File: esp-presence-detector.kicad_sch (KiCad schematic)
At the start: 6 parts, among them J1 AM312 female header, J2 LDR female header, U1 Wemos NodeMCU, U2 AM312

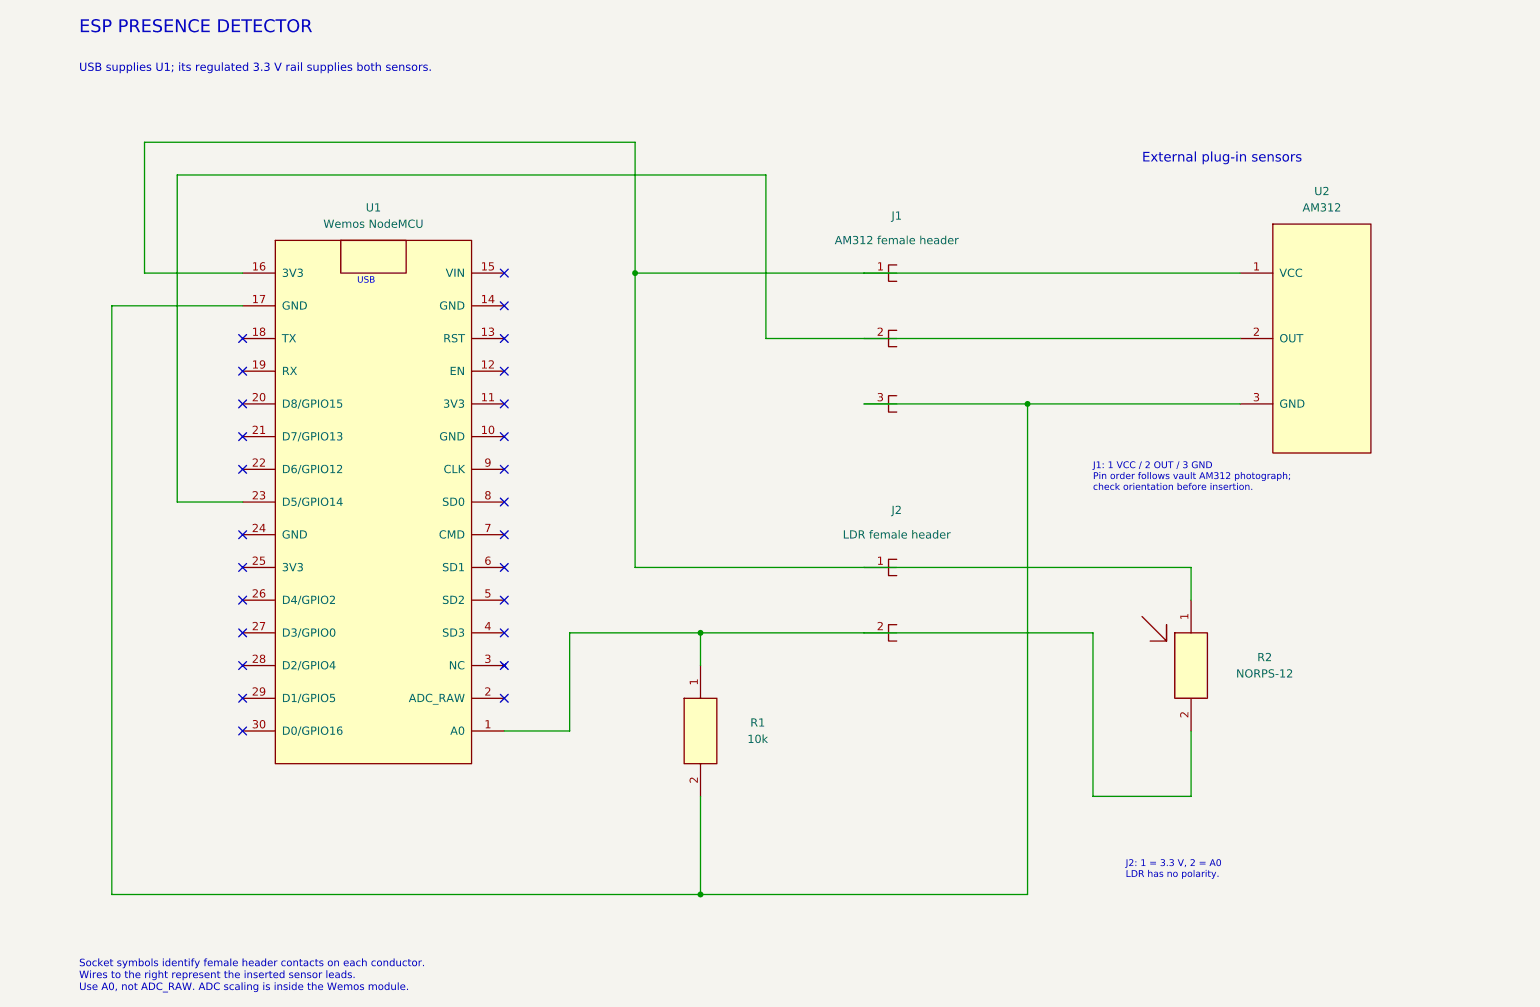
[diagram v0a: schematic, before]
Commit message: refactor: simplify schematic power and sensor connections
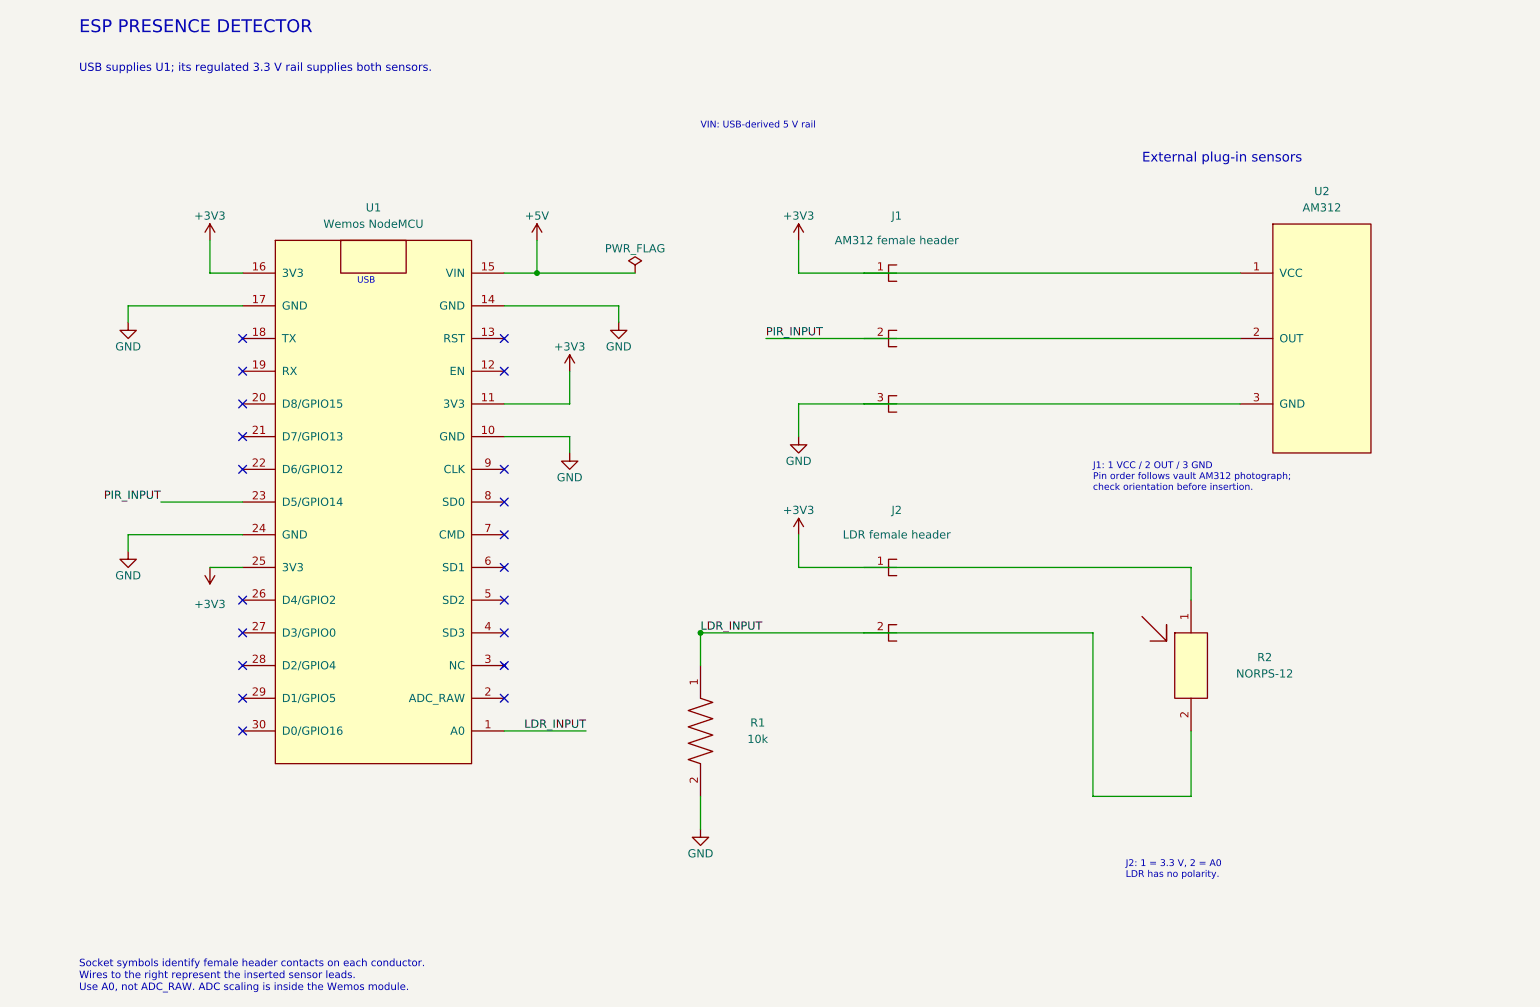
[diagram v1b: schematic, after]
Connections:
- net +3V3: now reaches J1.1, J2.1, R2.1, U1.16 (3V3), U2.1 (VCC)
- net +3V3: now also U1.11 (3V3), U1.25 (3V3)
- net PIR_INPUT: now reaches J1.2, U1.23 (D5/GPIO14), U2.2 (OUT)
- net GND: now reaches J1.3, R1.2, U1.17 (GND), U2.3 (GND)
- net GND: now also U1.10 (GND), U1.14 (GND), U1.24 (GND)
- net LDR_INPUT: now reaches J2.2, R1.1, R2.2, U1.1 (A0)
- net +5V: now reaches U1.15 (VIN)
- no-connect marks 26 -> 20
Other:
- note added: "VIN: USB-derived 5 V rail"

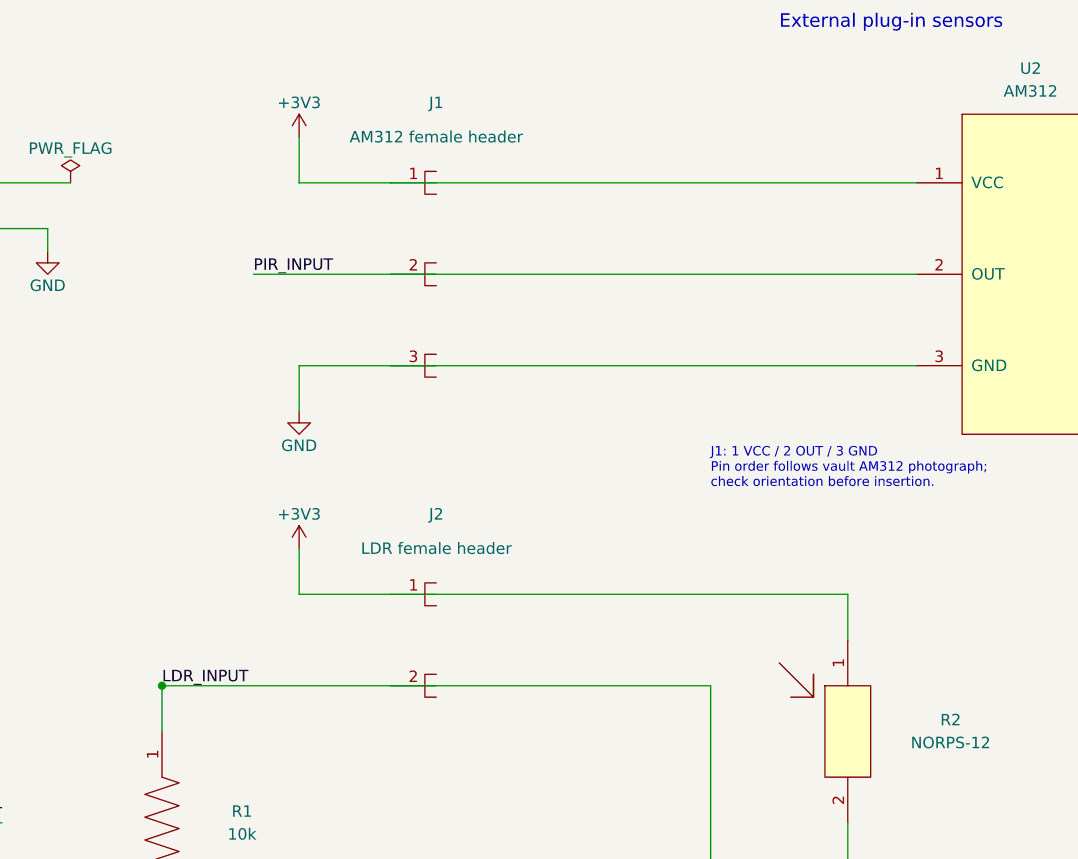
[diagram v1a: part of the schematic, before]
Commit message: refactor: use standard KiCad socket connectors
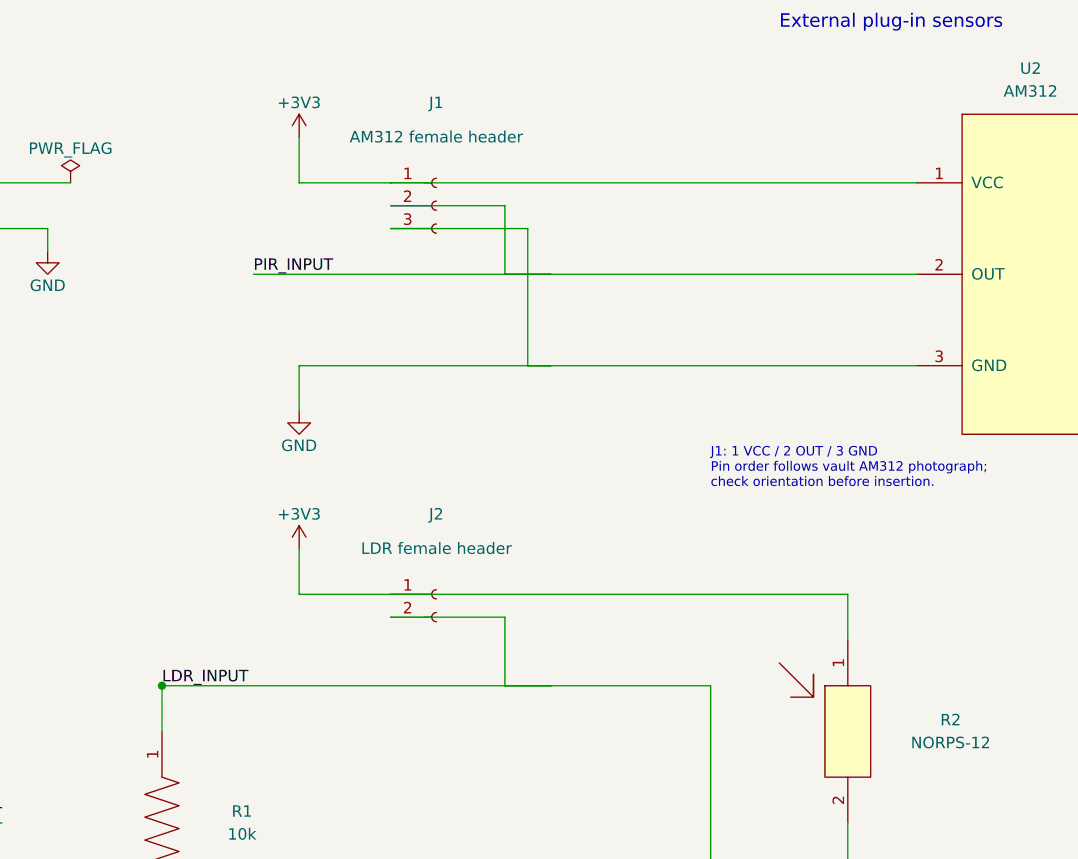
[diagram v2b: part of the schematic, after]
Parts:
- removed J1: AM312 female header, symbol Presence:Female_1x03
- removed J2: LDR female header, symbol Presence:Female_1x02
- added J1: AM312 female header, symbol Connector:Conn_01x03_Socket
- added J2: LDR female header, symbol Connector:Conn_01x02_Socket
- R1: symbol Presence:R -> R
- R2: symbol Presence:NORPS-12 -> NORPS-12
- U1: symbol Presence:Wemos_NodeMCU -> Wemos_NodeMCU
- U2: symbol Presence:AM312 -> AM312
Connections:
- net +3V3: now also J1.1 (Pin_1), J2.1 (Pin_1)
- net GND: now also J1.3 (Pin_3)
- net LDR_INPUT: now also J2.2 (Pin_2)
- net PIR_INPUT: now also J1.2 (Pin_2)

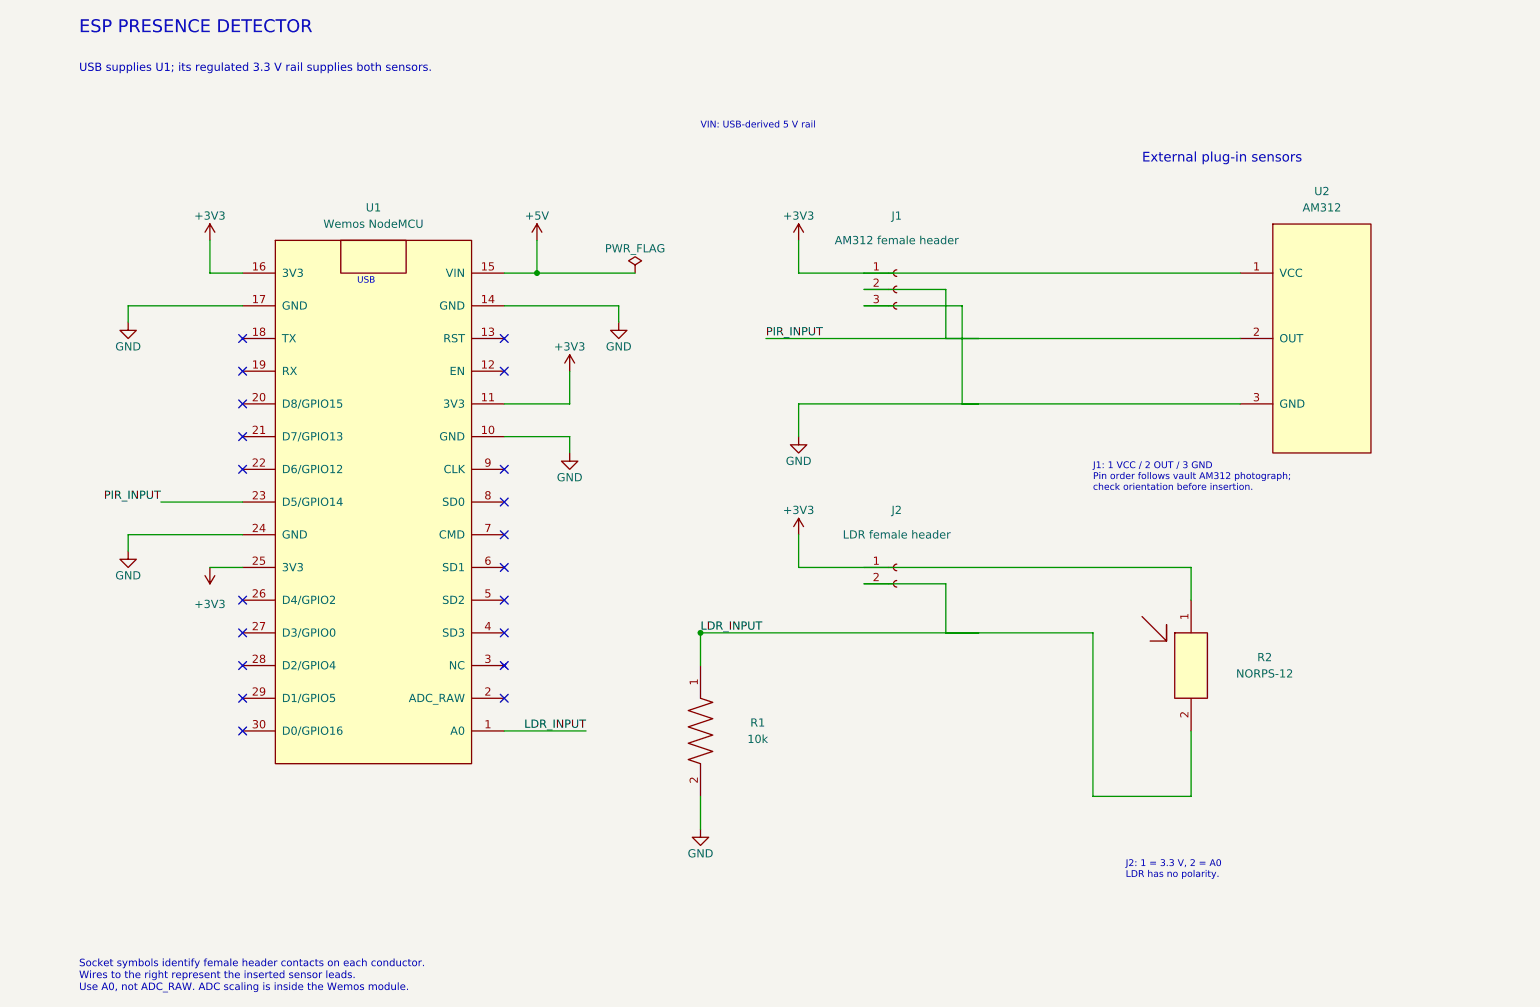
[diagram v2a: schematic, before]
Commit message: refactor: show off-board sensors and mating cable connectors
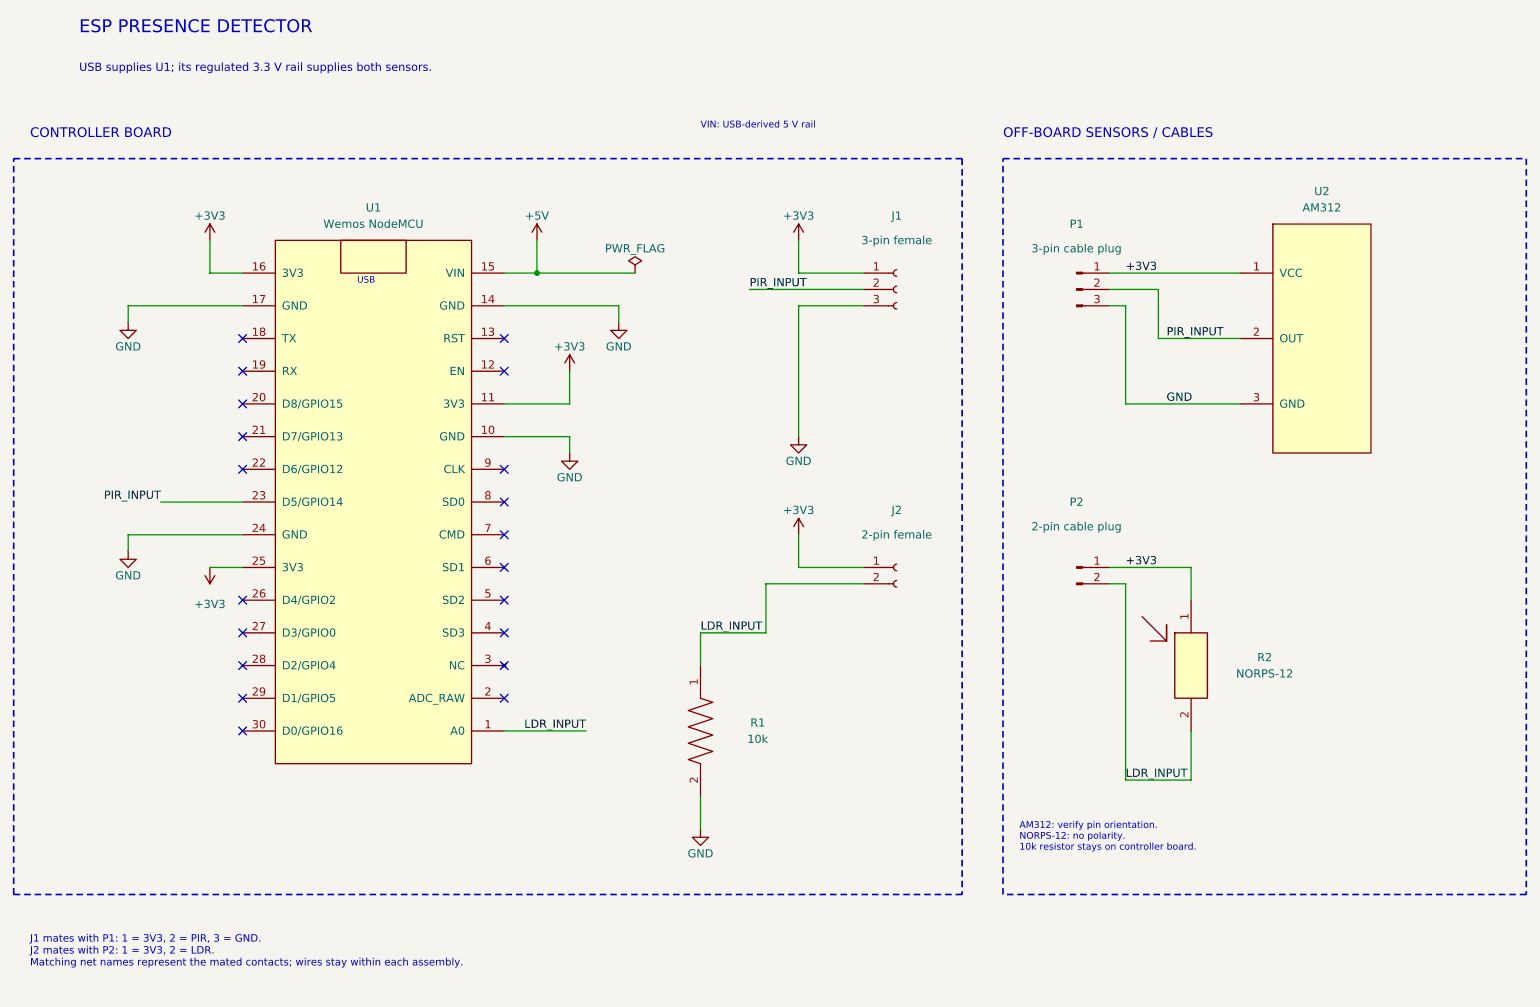
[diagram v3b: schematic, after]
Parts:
- added P1: 3-pin cable plug, symbol Connector:Conn_01x03_Pin
- added P2: 2-pin cable plug, symbol Connector:Conn_01x02_Pin
- J1: value AM312 female header -> 3-pin female
- J2: value LDR female header -> 2-pin female
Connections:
- net +3V3: now also P1.1 (Pin_1), P2.1 (Pin_1)
- net GND: now also P1.3 (Pin_3)
- net LDR_INPUT: now also P2.2 (Pin_2)
- net PIR_INPUT: now also P1.2 (Pin_2)
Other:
- note added: "AM312: verify pin orientation. NORPS-12: no polarity. 10k resistor stays on controller board."
- note added: "CONTROLLER BOARD"
- note added: "J1 mates with P1: 1 = 3V3, 2 = PIR, 3 = GND. J2 mates with P2: 1 = 3V3, 2 = LDR. Matching net names represent the mated contacts; wires stay within each assembly."
- note added: "OFF-BOARD SENSORS / CABLES"
- note removed: "External plug-in sensors"
- note removed: "J1: 1 VCC / 2 OUT / 3 GND Pin order follows vault AM312 photograph; check orientation before insertion."
- note removed: "J2: 1 = 3.3 V, 2 = A0 LDR has no polarity."
- note removed: "Socket symbols identify female header contacts on each conductor. Wires to the right represent the inserted sensor leads. Use A0, not ADC_RAW. ADC scaling is inside the Wemos module."
